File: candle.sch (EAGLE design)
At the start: 344 parts, among them U1 ATXMEGA_E5_TQFP, U2 SPW2430HR5H_B, U3 S25FL, U4 STP16CPC26TSSOP24

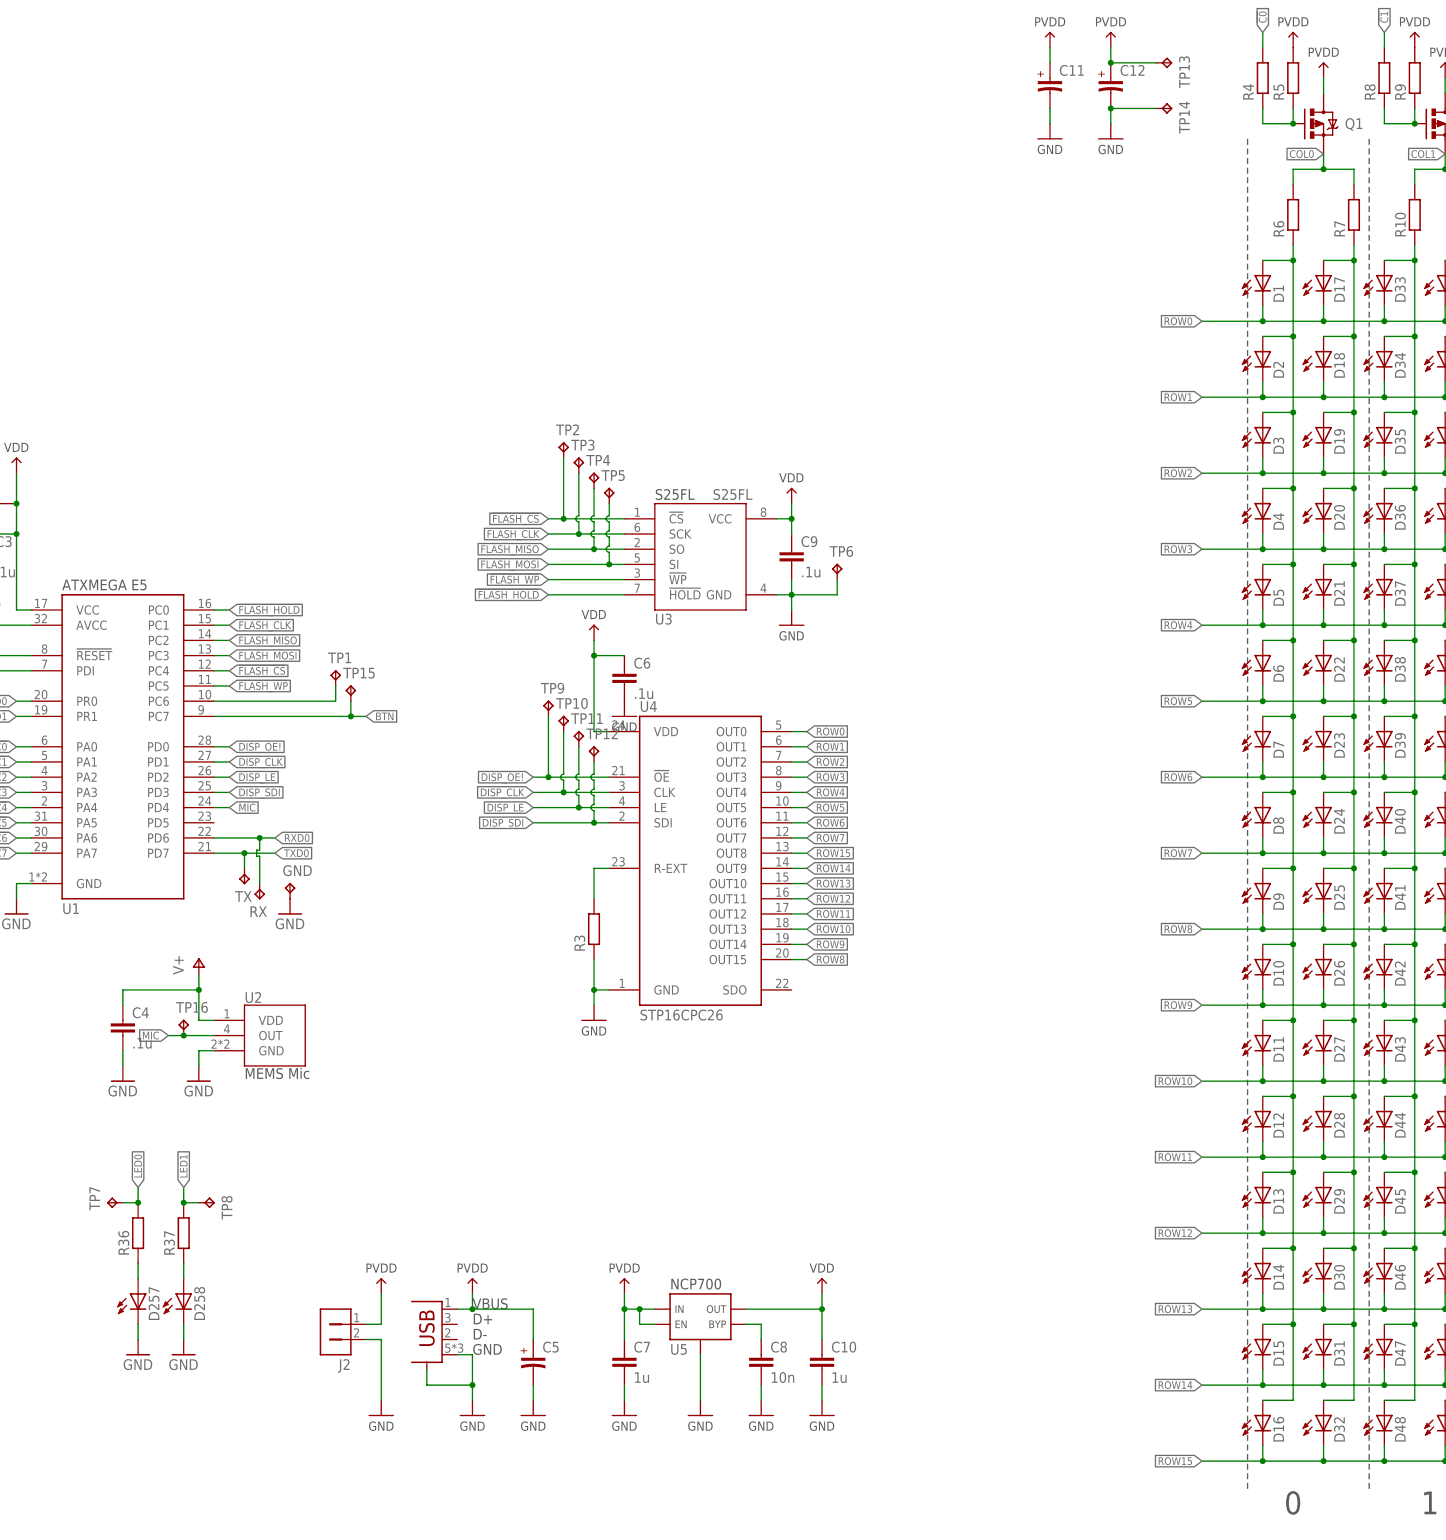
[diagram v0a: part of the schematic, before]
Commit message: Removed microphone and some connectors
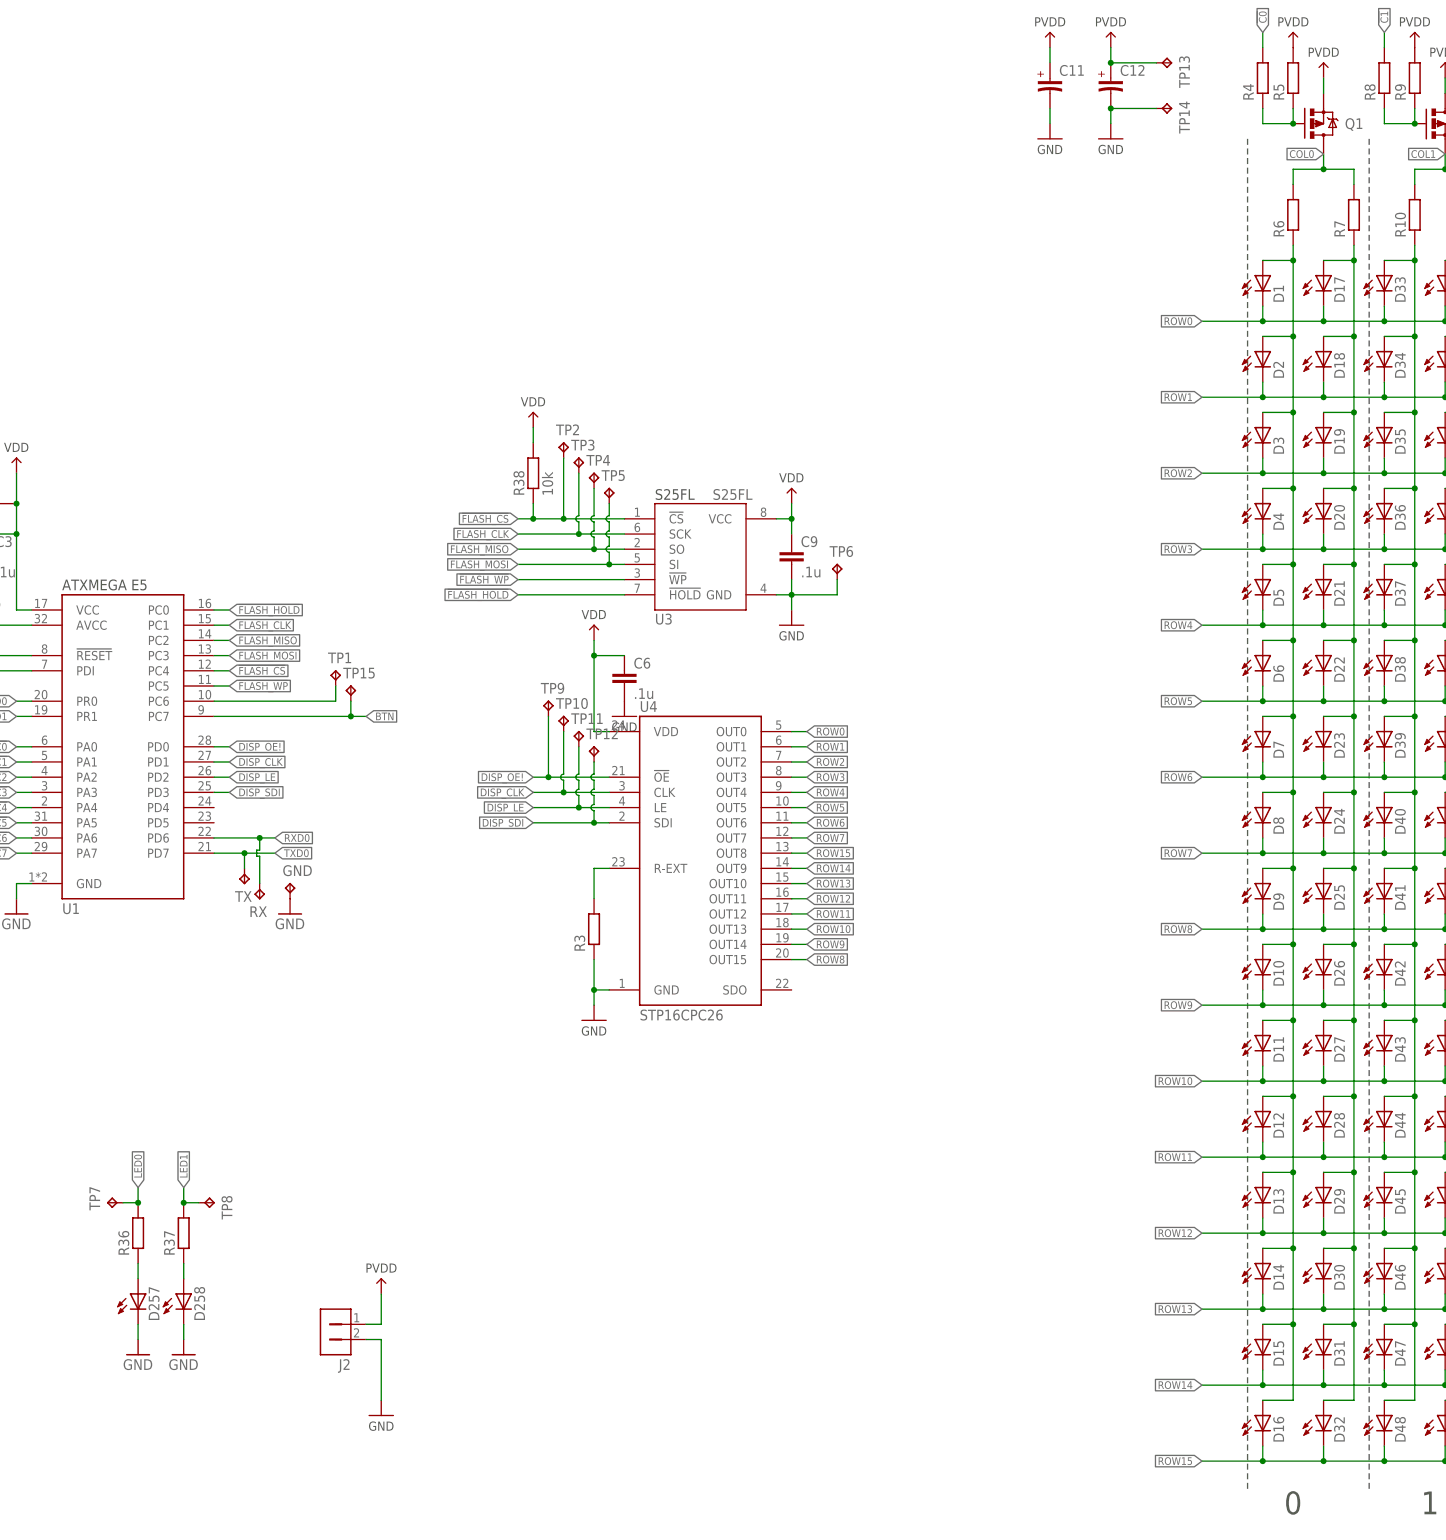
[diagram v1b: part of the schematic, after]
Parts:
- removed C10, C7: 1u, Sebastian:C_0805
- removed C4: .1u, Sebastian:C_0805
- removed C5: (no value), Sebastian:C_POL_1206
- removed C8: 10n, Sebastian:C_0805
- removed TP16: TPB1,27, testpad:TPB1,27
- removed U2: SPW2430HR5H_B, Sebastian:SPW2430HR5H_B
- removed U5: (no value), Sebastian 2:NCP700
- removed USB1: USB_MICRO_FCI_REAR_PEGS, Sebastian:USB_MICRO_FCI_REAR_PEGS
- added R38: 10k, Sebastian 2:R_0603
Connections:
- removed net MIC: TP16.TP, U1.PD4, U2.OUT
- removed net N$13: C8.1, U5.BYP
- net !FLASH_CS: now also R38.1
- net COL0: now also Q1.D; no longer Q1.S
- net GND: no longer C10.2, C4.2, C5.2, C7.2, C8.2, U2.GND, U5.GND, USB1.CASE, USB1.GND
- net PVDD: now also Q1.S; no longer C5.1, C7.1, Q1.D, U5.EN, U5.IN, USB1.VBUS
- net V+: no longer C4.1, U2.VDD
- net VDD: now also R38.2; no longer C10.1, U5.OUT
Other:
- moved on the sheet: Q1

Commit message: Fixed the transistor pinout error and updated eagle
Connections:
- net !C1_ renamed N$7
- net !C2_ renamed N$13
- net !C4_ renamed N$14
- net COL1: now also Q2.D; no longer Q2.S
- net COL2: now also Q3.D; no longer Q3.S
- net COL3: now also Q4.D; no longer Q4.S
- net COL4: now also Q5.D; no longer Q5.S
- net COL5: now also Q6.D; no longer Q6.S
- net COL6: now also Q7.D; no longer Q7.S
- net COL7: now also Q8.D; no longer Q8.S
- net PVDD: now also Q2.S, Q3.S, Q4.S, Q5.S, Q6.S, Q7.S, Q8.S; no longer Q2.D, Q3.D, Q4.D, Q5.D, Q6.D, Q7.D, Q8.D
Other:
- moved on the sheet: Q2, Q3, Q4, Q5, Q6, Q7, Q8

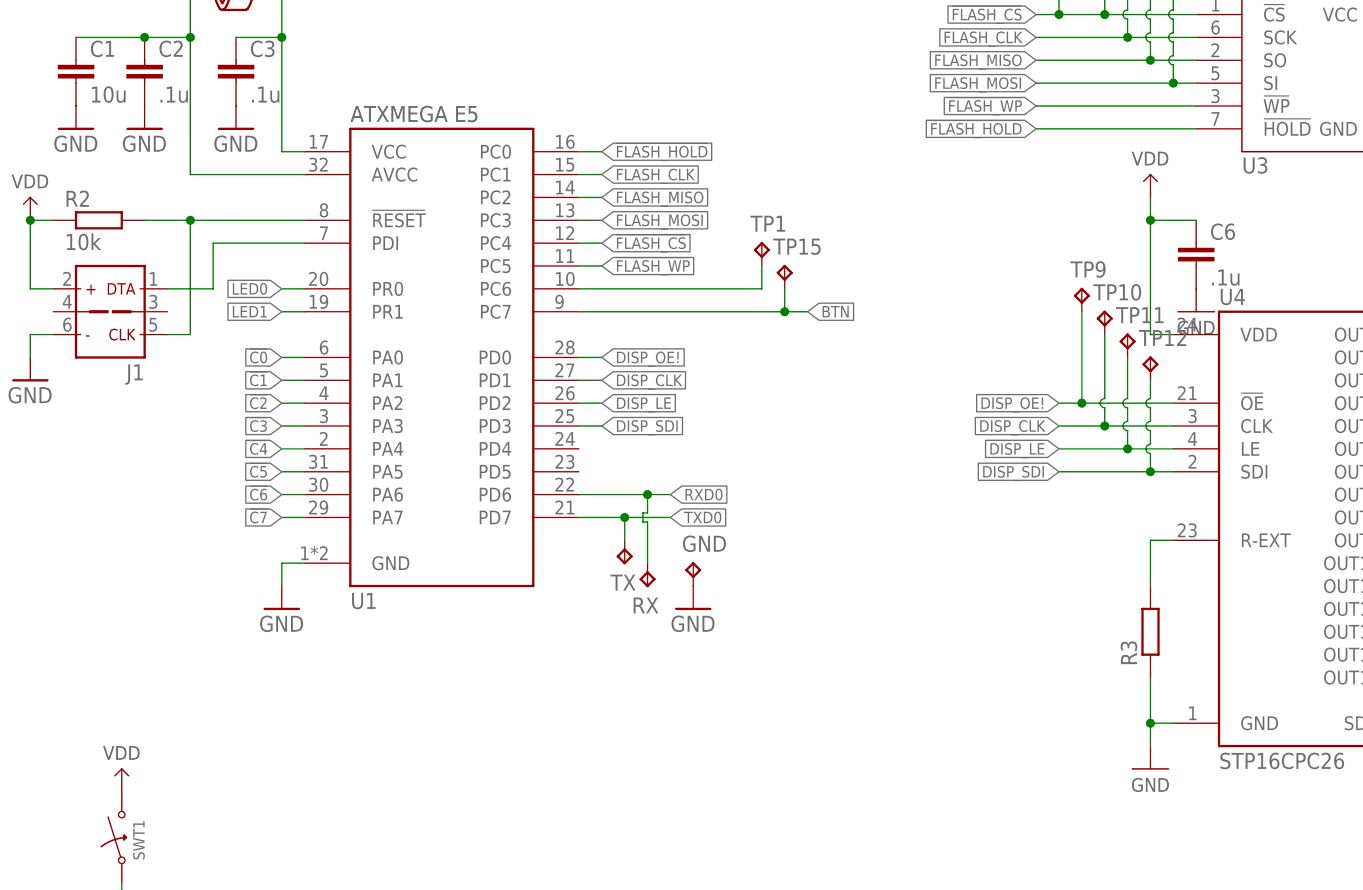
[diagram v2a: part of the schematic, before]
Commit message: Rewired the flash chip and rotated the mosfets
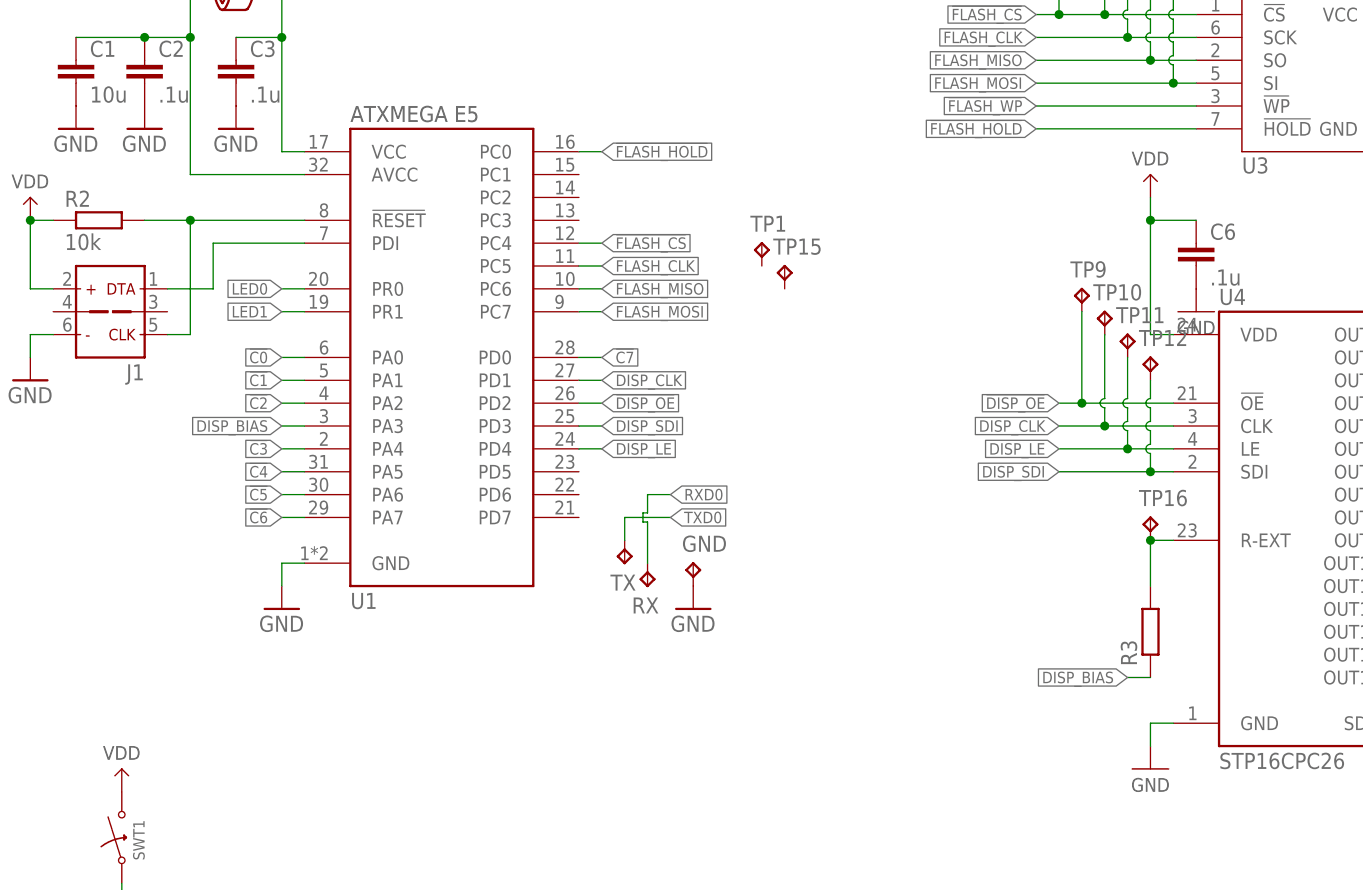
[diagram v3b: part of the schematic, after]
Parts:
- added TP16: TPB1,27, testpad:TPB1,27
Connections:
- removed net DISP_OE!: TP9.TP, U1.PD0, U4.!OE
- removed net N$6: TP1.TP, U1.PC6
- new net !DISP_OE: TP9.TP, U1.PD2, U4.!OE
- new net DISP_BIAS: R3.1, U1.PA3
- net !C3: now also U1.PA4; no longer U1.PA3
- net !C4: now also U1.PA5; no longer U1.PA4
- net !C5: now also U1.PA6; no longer U1.PA5
- net !C6: now also U1.PA7; no longer U1.PA6
- net !C7: now also U1.PD0; no longer U1.PA7
- net !FLASH_WP: no longer U1.PC5
- net BTN: no longer TP15.TP, U1.PC7
- net DISP_LE: now also U1.PD4; no longer U1.PD2
- net FLASH_CLK: now also U1.PC5; no longer U1.PC1
- net FLASH_MISO: now also U1.PC6; no longer U1.PC2
- net FLASH_MOSI: now also U1.PC7; no longer U1.PC3
- net GND: no longer R3.1
- net N$10: now also TP16.TP
- net RXD0: no longer U1.PD6
- net TXD0: no longer U1.PD7

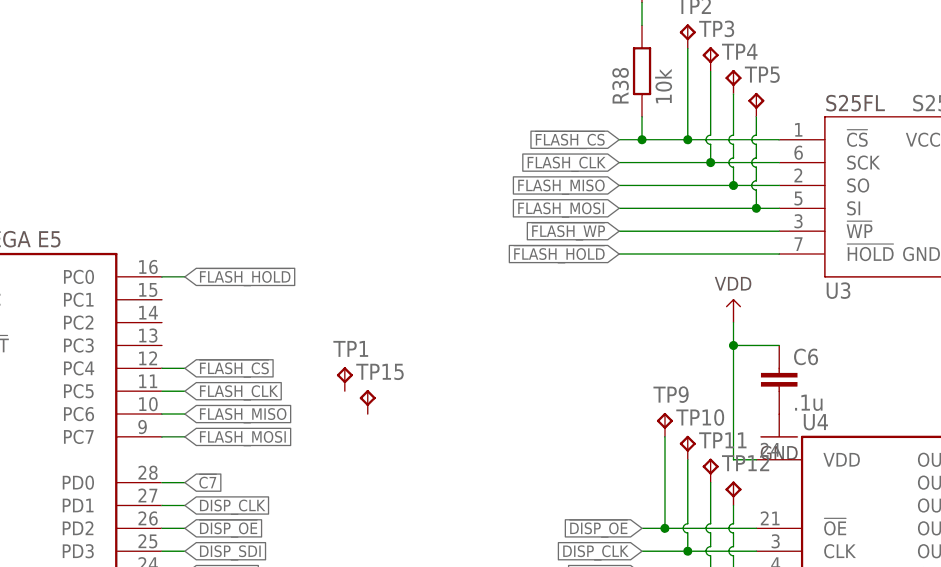
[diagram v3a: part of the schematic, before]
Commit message: Cleaned up the flash and removed unused pins
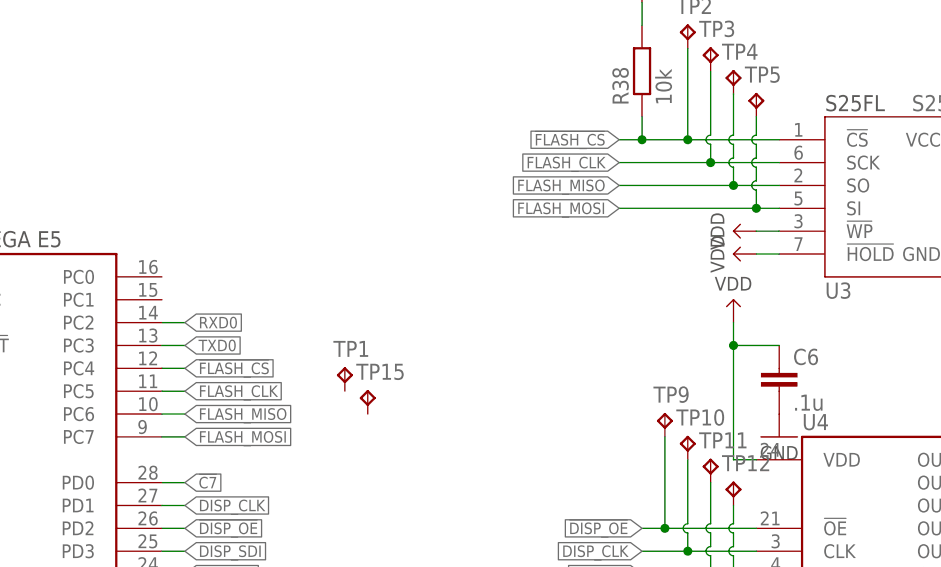
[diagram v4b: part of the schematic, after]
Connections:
- removed net !FLASH_HOLD: U1.PC0, U3.!HOLD
- removed net !FLASH_WP: U3.!WP
- net RXD0: now also U1.PC2
- net TXD0: now also U1.PC3
- net VDD: now also U3.!HOLD, U3.!WP
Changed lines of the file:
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@@
 <part name="P40" library="aesthetics" deviceset="VDD" device=""/>
 <part name="TP16" library="testpad" deviceset="TP" device="B1,27"/>
+<part name="P4" library="aesthetics" deviceset="VDD" device=""/>
+<part name="P5" library="aesthetics" deviceset="VDD" device=""/>
 </parts>
 <sheets>
@@
 <instance part="P40" gate="G$1" x="-78.74" y="38.1"/>
 <instance part="TP16" gate="G$1" x="-68.58" y="-33.02"/>
+<instance part="P4" gate="G$1" x="-66.04" y="12.7" rot="R90"/>
+<instance part="P5" gate="G$1" x="-66.04" y="10.16" rot="R90"/>
 </instances>
 <busses>
@@
 <pinref part="P40" gate="G$1" pin="VDD"/>
 </segment>
+<segment>
+<pinref part="U3" gate="G$1" pin="!WP"/>
+<wire x1="-63.5" y1="12.7" x2="-66.04" y2="12.7" width="0.1524" layer="91"/>
+<pinref part="P4" gate="G$1" pin="VDD"/>
+</segment>
+<segment>
+<pinref part="U3" gate="G$1" pin="!HOLD"/>
+<wire x1="-63.5" y1="10.16" x2="-66.04" y2="10.16" width="0.1524" layer="91"/>
+<pinref part="P5" gate="G$1" pin="VDD"/>
+</segment>
 </net>
 <net name="DISP_CLK" class="0">
@@
 <label x="-121.92" y="-33.02" size="1.27" layer="95" font="vector" xref="yes"/>
 </segment>
+<segment>
+<pinref part="U1" gate="G$1" pin="PC3"/>
+<wire x1="-132.08" y1="0" x2="-129.54" y2="0" width="0.1524" layer="91"/>
+<label x="-129.54" y="0" size="1.27" layer="95" font="vector" xref="yes"/>
+</segment>
 </net>
 <net name="!RESET" class="0">
@@
 </segment>
 </net>
-<net name="!FLASH_WP" class="0">
-<segment>
-<pinref part="U3" gate="G$1" pin="!WP"/>
-<wire x1="-63.5" y1="12.7" x2="-81.28" y2="12.7" width="0.1524" layer="91"/>
-<label x="-81.28" y="12.7" size="1.27" layer="95" font="vector" rot="R180" xref="yes"/>
-</segment>
-</net>
-<net name="!FLASH_HOLD" class="0">
-<segment>
-<pinref part="U3" gate="G$1" pin="!HOLD"/>
-<wire x1="-63.5" y1="10.16" x2="-81.28" y2="10.16" width="0.1524" layer="91"/>
-<label x="-81.28" y="10.16" size="1.27" layer="95" font="vector" rot="R180" xref="yes"/>
-</segment>
-<segment>
-<pinref part="U1" gate="G$1" pin="PC0"/>
-<wire x1="-132.08" y1="7.62" x2="-129.54" y2="7.62" width="0.1524" layer="91"/>
-<label x="-129.54" y="7.62" size="1.27" layer="95" font="vector" xref="yes"/>
-</segment>
-</net>
 <net name="RXD0" class="0">
 <segment>
@@
 <label x="-121.92" y="-30.48" size="1.27" layer="95" font="vector" xref="yes"/>
 </segment>
+<segment>
+<pinref part="U1" gate="G$1" pin="PC2"/>
+<wire x1="-132.08" y1="2.54" x2="-129.54" y2="2.54" width="0.1524" layer="91"/>
+<label x="-129.54" y="2.54" size="1.27" layer="95" font="vector" xref="yes"/>
+</segment>
 </net>
